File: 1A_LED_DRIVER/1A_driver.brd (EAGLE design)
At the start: 160 x 100 mm, 1 part

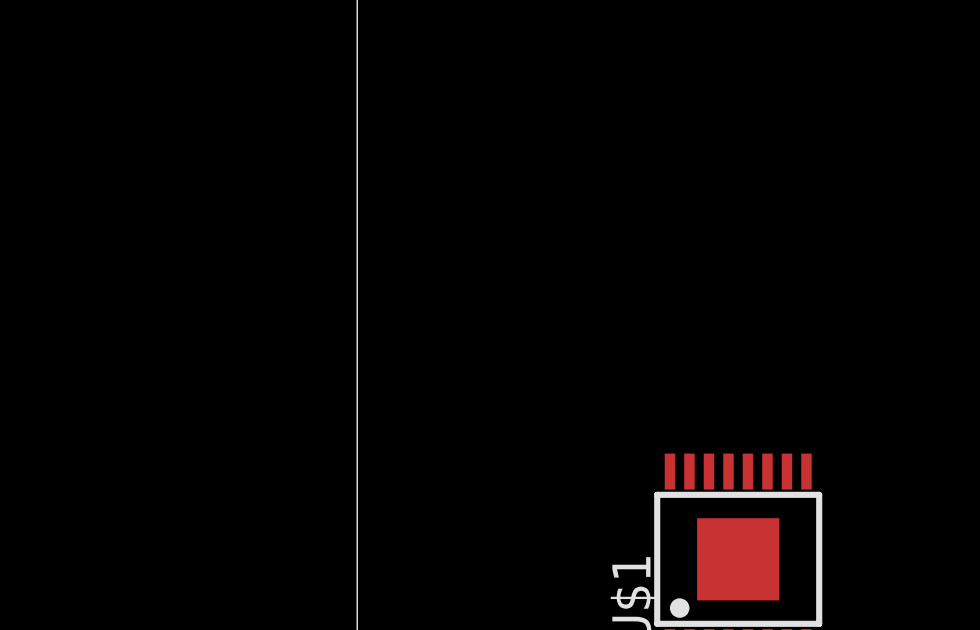
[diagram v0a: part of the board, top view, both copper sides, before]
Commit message: making new mosfet lib
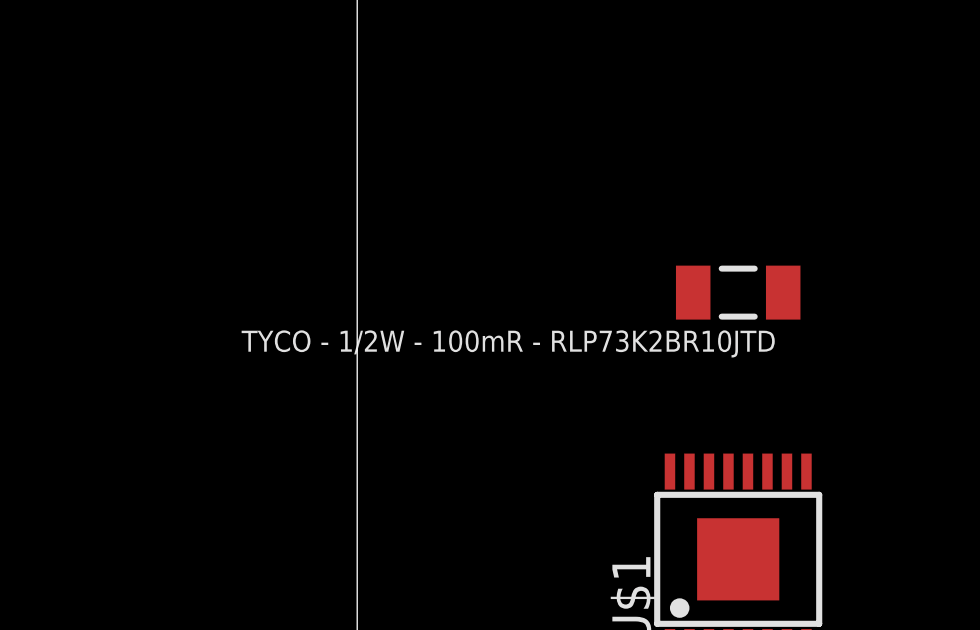
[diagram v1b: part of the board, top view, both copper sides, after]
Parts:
- added R1: TYCO - 1/2W - 100mR - RLP73K2BR10JTD, standard_passive:R1206
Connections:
- new net N$1: R1.2, U$1.13
- new net N$2: R1.1, U$1.12
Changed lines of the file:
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@@
 <elements>
 <element name="U$1" library="LT3517" package="TSSOP16_PAD" value="LT3517_TSSOP" x="12.7" y="13.97"/>
+<element name="R1" library="standard_passive" package="R1206" value="TYCO - 1/2W - 100mR - RLP73K2BR10JTD" x="12.7" y="22.86" rot="R180"/>
 </elements>
 <signals>
@@
 <contactref element="U$1" pad="17"/>
 </signal>
+<signal name="N$1">
+<contactref element="U$1" pad="13"/>
+<contactref element="R1" pad="2"/>
+<wire x1="11.2" y1="22.86" x2="12.375" y2="16.895" width="0" layer="19" extent="1-1"/>
+</signal>
+<signal name="N$2">
+<contactref element="U$1" pad="12"/>
+<contactref element="R1" pad="1"/>
+<wire x1="14.2" y1="22.86" x2="13.025" y2="16.895" width="0" layer="19" extent="1-1"/>
+</signal>
 </signals>

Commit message: schematic finished
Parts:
- added C1, C2: 0.1u, standard_passive:R0603
- added C3: 4.7u, standard_passive:R1206
- added C4: 0.22u, standard_passive:R0603
- added D1: RB060MM-60TF, DIODES:SOD123FL
- added L1: 6.8u, WE-PD:WE-PD_1260/1245/1280/1210
- added Q1: ZXMP6A13FTA, MOSFET:SOT23
- added R2, R3, R4, R5: (no value), standard_passive:R0603
- added R6: 6.04k, standard_passive:R0603
- added SV1: (no value), con-lstb:MA04-1
- added X1: 22-23-2021, con-molex:22-23-2021
- R1: value TYCO - 1/2W - 100mR - RLP73K2BR10JTD -> 100mR - 1/2W
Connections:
- new net N$10: C1.1, U$1.9
- new net N$11: R6.1, U$1.4
- new net N$3: Q1.G, U$1.14
- new net N$4: D1.A, L1.2, U$1.15, U$1.16
- new net N$5: Q1.D, X1.1
- new net N$6: R2.1, R3.2, U$1.10
- new net N$8: C2.2, U$1.6
- new net N$9: R4.2, R5.1, U$1.8
- new net PWM: SV1.3, U$1.7
- new net VIN: C3.1, L1.1, SV1.4, U$1.1, U$1.2, X1.2
- new net VREF: R4.1, U$1.11, U$1.3
- net GND: now also C1.2, C2.1, C4.2, R3.1, R5.2, R6.2, SV1.1, SV1.2, U$1.5
- net N$1: now also C3.2, C4.1, D1.C, R2.2
- net N$2: now also Q1.S
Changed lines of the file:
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@@
 <layer number="48" name="Document" color="7" fill="1" visible="yes" active="yes"/>
 <layer number="49" name="Reference" color="7" fill="1" visible="yes" active="yes"/>
+<layer number="50" name="dxf" color="7" fill="1" visible="no" active="no"/>
 <layer number="51" name="tDocu" color="7" fill="1" visible="yes" active="yes"/>
 <layer number="52" name="bDocu" color="7" fill="1" visible="yes" active="yes"/>
+<layer number="53" name="tPadExt" color="7" fill="1" visible="no" active="no"/>
+<layer number="54" name="bPadExt" color="1" fill="1" visible="no" active="no"/>
 <layer number="90" name="Modules" color="5" fill="1" visible="no" active="no"/>
 <layer number="91" name="Nets" color="2" fill="1" visible="no" active="no"/>
@@
 <layer number="97" name="Info" color="7" fill="1" visible="no" active="no"/>
 <layer number="98" name="Guide" color="6" fill="1" visible="no" active="no"/>
+<layer number="99" name="SpiceOrder" color="5" fill="1" visible="no" active="no"/>
+<layer number="250" name="Descript" color="3" fill="1" visible="no" active="no"/>
+<layer number="251" name="SMDround" color="12" fill="11" visible="no" active="no"/>
 </layers>
 <board>
@@
 <elements>
 <element name="U$1" library="LT3517" package="TSSOP16_PAD" value="LT3517_TSSOP" x="12.7" y="13.97"/>
-<element name="R1" library="standard_passive" package="R1206" value="TYCO - 1/2W - 100mR - RLP73K2BR10JTD" x="12.7" y="22.86" rot="R180"/>
+<element name="R1" library="standard_passive" package="R1206" value="100mR - 1/2W" x="12.7" y="22.86" rot="R180"/>
+<element name="Q1" library="MOSFET" package="SOT23" value="ZXMP6A13FTA" x="-2.54" y="-3.81"/>
+<element name="D1" library="DIODES" package="SOD123FL" value="RB060MM-60TF" x="-2.54" y="-10.16"/>
+<element name="X1" library="con-molex" package="22-23-2021" value="22-23-2021" x="3.81" y="-21.59">
+<attribute name="OC_FARNELL" value="1462926" x="3.81" y="-21.59" size="1.778" layer="27" display="off"/>
+<attribute name="OC_NEWARK" value="25C3832" x="3.81" y="-21.59" size="1.778" layer="27" display="off"/>
+<attribute name="MPN" value="22-23-2021" x="3.81" y="-21.59" size="1.778" layer="27" display="off"/>
+<attribute name="MF" value="MOLEX" x="3.81" y="-21.59" size="1.778" layer="27" display="off"/>
+</element>
+<element name="R2" library="standard_passive" package="R0603" value="" x="-8.89" y="-25.4"/>
+<element name="R3" library="standard_passive" package="R0603" value="" x="-13.97" y="-25.4"/>
+<element name="L1" library="WE-PD" package="WE-PD_1260/1245/1280/1210" value="6.8u" x="-22.86" y="-19.05">
+<attribute name="OC_FARNELL" value="2211534" x="-22.86" y="-19.05" size="1.778" layer="27" display="off"/>
+<attribute name="OC_NEWARK" value="44W4713" x="-22.86" y="-19.05" size="1.778" layer="27" display="off"/>
+<attribute name="SUPPLIER" value="Wuerth Elektronik" x="-22.86" y="-19.05" size="1.778" layer="27" display="off"/>
+<attribute name="MPN" value="744771006" x="-22.86" y="-19.05" size="1.778" layer="27" display="off"/>
+<attribute name="PACKAGE" value="1260" x="-22.86" y="-19.05" size="1.778" layer="27" display="off"/>
+</element>
+<element name="R4" library="standard_passive" package="R0603" value="" x="-33.02" y="-25.4"/>
+<element name="R5" library="standard_passive" package="R0603" value="" x="-38.1" y="-25.4"/>
+<element name="C1" library="standard_passive" package="R0603" value="0.1u" x="-43.18" y="-25.4"/>
+<element name="C2" library="standard_passive" package="R0603" value="0.1u" x="-48.26" y="-25.4"/>
+<element name="R6" library="standard_passive" package="R0603" value="6.04k" x="-53.34" y="-25.4"/>
+<element name="C3" library="standard_passive" package="R1206" value="4.7u" x="-58.42" y="-25.4"/>
+<element name="C4" library="standard_passive" package="R0603" value="0.22u" x="-63.5" y="-25.4"/>
+<element name="SV1" library="con-lstb" package="MA04-1" value="" x="-53.34" y="-36.83">
+<attribute name="OC_FARNELL" value="unknown" x="-53.34" y="-36.83" size="1.778" layer="27" display="off"/>
+<attribute name="OC_NEWARK" value="unknown" x="-53.34" y="-36.83" size="1.778" layer="27" display="off"/>
+<attribute name="MPN" value="" x="-53.34" y="-36.83" size="1.778" layer="27" display="off"/>
+<attribute name="MF" value="" x="-53.34" y="-36.83" size="1.778" layer="27" display="off"/>
+</element>
 </elements>
 <signals>
 <signal name="GND">
 <contactref element="U$1" pad="17"/>
+<contactref element="R3" pad="1"/>
+<contactref element="R5" pad="2"/>
+<contactref element="C2" pad="1"/>
+<contactref element="C1" pad="2"/>
+<contactref element="R6" pad="2"/>
+<contactref element="U$1" pad="5"/>
+<contactref element="C4" pad="2"/>
+<contactref element="SV1" pad="1"/>
+<contactref element="SV1" pad="2"/>
+<wire x1="-54.61" y1="-36.83" x2="-57.15" y2="-36.83" width="0" layer="19" extent="1-1"/>
+<wire x1="-52.54" y1="-25.4" x2="-54.61" y2="-36.83" width="0" layer="19" extent="1-1"/>
+<wire x1="-49.06" y1="-25.4" x2="-52.54" y2="-25.4" width="0" layer="19" extent="1-1"/>
+<wire x1="-42.38" y1="-25.4" x2="-49.06" y2="-25.4" width="0" layer="19" extent="1-1"/>
+<wire x1="-37.3" y1="-25.4" x2="-42.38" y2="-25.4" width="0" layer="19" extent="1-1"/>
+<wire x1="-62.7" y1="-25.4" x2="-52.54" y2="-25.4" width="0" layer="19" extent="1-1"/>
+<wire x1="-14.77" y1="-25.4" x2="-37.3" y2="-25.4" width="0" layer="19" extent="1-1"/>
+<wire x1="13.025" y1="11.045" x2="-14.77" y2="-25.4" width="0" layer="19" extent="1-1"/>
+<wire x1="12.7" y1="13.97" x2="13.025" y2="11.045" width="0" layer="19" extent="1-1"/>
 </signal>
 <signal name="N$1">
 <contactref element="U$1" pad="13"/>
 <contactref element="R1" pad="2"/>
+<contactref element="D1" pad="C"/>
+<contactref element="R2" pad="2"/>
+<contactref element="C3" pad="2"/>
+<contactref element="C4" pad="1"/>
+<wire x1="-56.92" y1="-25.4" x2="-64.3" y2="-25.4" width="0" layer="19" extent="1-1"/>
+<wire x1="-8.09" y1="-25.4" x2="-56.92" y2="-25.4" width="0" layer="19" extent="1-1"/>
+<wire x1="-4.165" y1="-10.16" x2="-8.09" y2="-25.4" width="0" layer="19" extent="1-1"/>
+<wire x1="12.375" y1="16.895" x2="-4.165" y2="-10.16" width="0" layer="19" extent="1-1"/>
 <wire x1="11.2" y1="22.86" x2="12.375" y2="16.895" width="0" layer="19" extent="1-1"/>
 </signal>
@@
 <contactref element="U$1" pad="12"/>
 <contactref element="R1" pad="1"/>
-<wire x1="14.2" y1="22.86" x2="13.025" y2="16.895" width="0" layer="19" extent="1-1"/>
+<contactref element="Q1" pad="S"/>
+<wire x1="13.025" y1="16.895" x2="14.2" y2="22.86" width="0" layer="19" extent="1-1"/>
+<wire x1="-1.59" y1="-4.91" x2="13.025" y2="16.895" width="0" layer="19" extent="1-1"/>
+</signal>
+<signal name="N$3">
+<contactref element="U$1" pad="14"/>
+<contactref element="Q1" pad="G"/>
+<wire x1="-3.49" y1="-4.91" x2="11.725" y2="16.895" width="0" layer="19" extent="1-1"/>
+</signal>
+<signal name="N$4">
+<contactref element="D1" pad="A"/>
+<contactref element="U$1" pad="16"/>
+<contactref element="U$1" pad="15"/>
+<contactref element="L1" pad="2"/>
+<wire x1="-0.915" y1="-10.16" x2="-17.91" y2="-19.05" width="0" layer="19" extent="1-1"/>
+<wire x1="10.425" y1="16.895" x2="-0.915" y2="-10.16" width="0" layer="19" extent="1-1"/>
+<wire x1="11.075" y1="16.895" x2="10.425" y2="16.895" width="0" layer="19" extent="1-1"/>
+</signal>
+<signal name="N$5">
+<contactref element="Q1" pad="D"/>
+<contactref element="X1" pad="1"/>
+<wire x1="-2.54" y1="-2.71" x2="2.54" y2="-21.59" width="0" layer="19" extent="1-1"/>
+</signal>
+<signal name="N$6">
+<contactref element="U$1" pad="10"/>
+<contactref element="R3" pad="2"/>
+<contactref element="R2" pad="1"/>
+<wire x1="-9.69" y1="-25.4" x2="-13.17" y2="-25.4" width="0" layer="19" extent="1-1"/>
+<wire x1="14.325" y1="16.895" x2="-9.69" y2="-25.4" width="0" layer="19" extent="1-1"/>
+</signal>
+<signal name="VIN">
+<contactref element="L1" pad="1"/>
+<contactref element="U$1" pad="1"/>
+<contactref element="U$1" pad="2"/>
+<contactref element="X1" pad="2"/>
+<contactref element="C3" pad="1"/>
+<contactref element="SV1" pad="4"/>
+<wire x1="-49.53" y1="-36.83" x2="-59.92" y2="-25.4" width="0" layer="19" extent="1-1"/>
+<wire x1="-27.81" y1="-19.05" x2="-49.53" y2="-36.83" width="0" layer="19" extent="1-1"/>
+<wire x1="5.08" y1="-21.59" x2="-27.81" y2="-19.05" width="0" layer="19" extent="1-1"/>
+<wire x1="10.425" y1="11.045" x2="5.08" y2="-21.59" width="0" layer="19" extent="1-1"/>
+<wire x1="11.075" y1="11.045" x2="10.425" y2="11.045" width="0" layer="19" extent="1-1"/>
+</signal>
+<signal name="VREF">
+<contactref element="U$1" pad="3"/>
+<contactref element="R4" pad="1"/>
+<contactref element="U$1" pad="11"/>
+<wire x1="11.725" y1="11.045" x2="-33.82" y2="-25.4" width="0" layer="19" extent="1-1"/>
+<wire x1="13.675" y1="16.895" x2="11.725" y2="11.045" width="0" layer="19" extent="1-1"/>
+</signal>
+<signal name="N$9">
+<contactref element="U$1" pad="8"/>
+<contactref element="R4" pad="2"/>
+<contactref element="R5" pad="1"/>
+<wire x1="-32.22" y1="-25.4" x2="-38.9" y2="-25.4" width="0" layer="19" extent="1-1"/>
+<wire x1="14.975" y1="11.045" x2="-32.22" y2="-25.4" width="0" layer="19" extent="1-1"/>
+</signal>
+<signal name="N$8">
+<contactref element="U$1" pad="6"/>
+<contactref element="C2" pad="2"/>
+<wire x1="13.675" y1="11.045" x2="-47.46" y2="-25.4" width="0" layer="19" extent="1-1"/>
+</signal>
+<signal name="N$10">
+<contactref element="U$1" pad="9"/>
+<contactref element="C1" pad="1"/>
+<wire x1="14.975" y1="16.895" x2="-43.98" y2="-25.4" width="0" layer="19" extent="1-1"/>
+</signal>
+<signal name="N$11">
+<contactref element="R6" pad="1"/>
+<contactref element="U$1" pad="4"/>
+<wire x1="12.375" y1="11.045" x2="-54.14" y2="-25.4" width="0" layer="19" extent="1-1"/>
+</signal>
+<signal name="PWM">
+<contactref element="SV1" pad="3"/>
+<contactref element="U$1" pad="7"/>
+<wire x1="14.325" y1="11.045" x2="-52.07" y2="-36.83" width="0" layer="19" extent="1-1"/>
 </signal>
 </signals>

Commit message: need to finish layout for the 1A regulator
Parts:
- added C5: 4.7u, standard_passive:R1206
- added C7: 100u, rcl:E5-5
- moved C4 98.1 mm to (19.7, 26.7)
- moved C3 89.7 mm to (14.6, 26.7)
- moved SV1 84.1 mm to (21.0, 2.54), turned to 180 degrees
- moved C1 80.5 mm to (24.8, 17.8)
- moved R6 80.1 mm to (18.4, 10.2), turned to 180 degrees
- moved C2 78.9 mm to (22.2, 10.2), turned to 180 degrees
- moved R5 69.6 mm to (22.9, 8.26)
- moved R4 62.5 mm to (19.7, 8.26)
- moved R3 59.4 mm to (24.8, 19.7), turned to 180 degrees
- moved R2 57.8 mm to (24.8, 21.6), turned to 180 degrees
- moved X1 52.8 mm to (30.2, 24.1), turned to 270 degrees
- moved L1 46.3 mm to (8.26, 15.2), turned to 90 degrees
- moved Q1 39.6 mm to (24.1, 25.4), turned to 270 degrees
- moved D1 38.3 mm to (14.6, 24.1), turned to 180 degrees
- moved R1 7.10 mm to (19.7, 24.1)
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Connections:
- net N$1 renamed I_P
- net N$2 renamed I_N
- net N$5 renamed I_LED
- net GND: now also C5.1, C7.-
- net VIN: now also C5.2, C7.+
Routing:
- net I_N: track 0.00 -> 7.01 mm
- net I_P: track 0.00 -> 7.01 mm
- added copper zone on layer 2, net GND
- added copper zone on layer 1, net I_N
- added copper zone on layer 1, net I_P
- added copper zone on layer 1, net N$1
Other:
- board size 160 x 100 mm -> 40 x 30 mm

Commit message: almost finished led drvier
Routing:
- net VREF: track 0.00 -> 23.1 mm, vias 0 -> 2
- net N$3: track 0.00 -> 11.4 mm, vias 0 -> 2
- net I_P: track 7.01 -> 15.8 mm, vias 0 -> 2
- net GND: track 0.00 -> 8.67 mm, vias 9 -> 18
- net N$6: track 0.00 -> 6.58 mm
- net N$9: track 0.00 -> 4.28 mm
- net N$8: track 0.00 -> 2.58 mm
- net N$11: track 0.00 -> 2.22 mm
- net N$10: track 0.00 -> 2.16 mm
- net VIN: track 0.00 -> 1.04 mm, vias 0 -> 21
- added copper zone on layer 1, net GND
- added copper zone on layer 1, net I_LED
- added copper zone on layer 1, net N$4
- added copper zone on layer 1, net VIN
- added copper zone on layer 15, net VIN
- removed copper zone on layer 1, net N$1
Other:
- board size 40 x 30 mm -> 35 x 30 mm

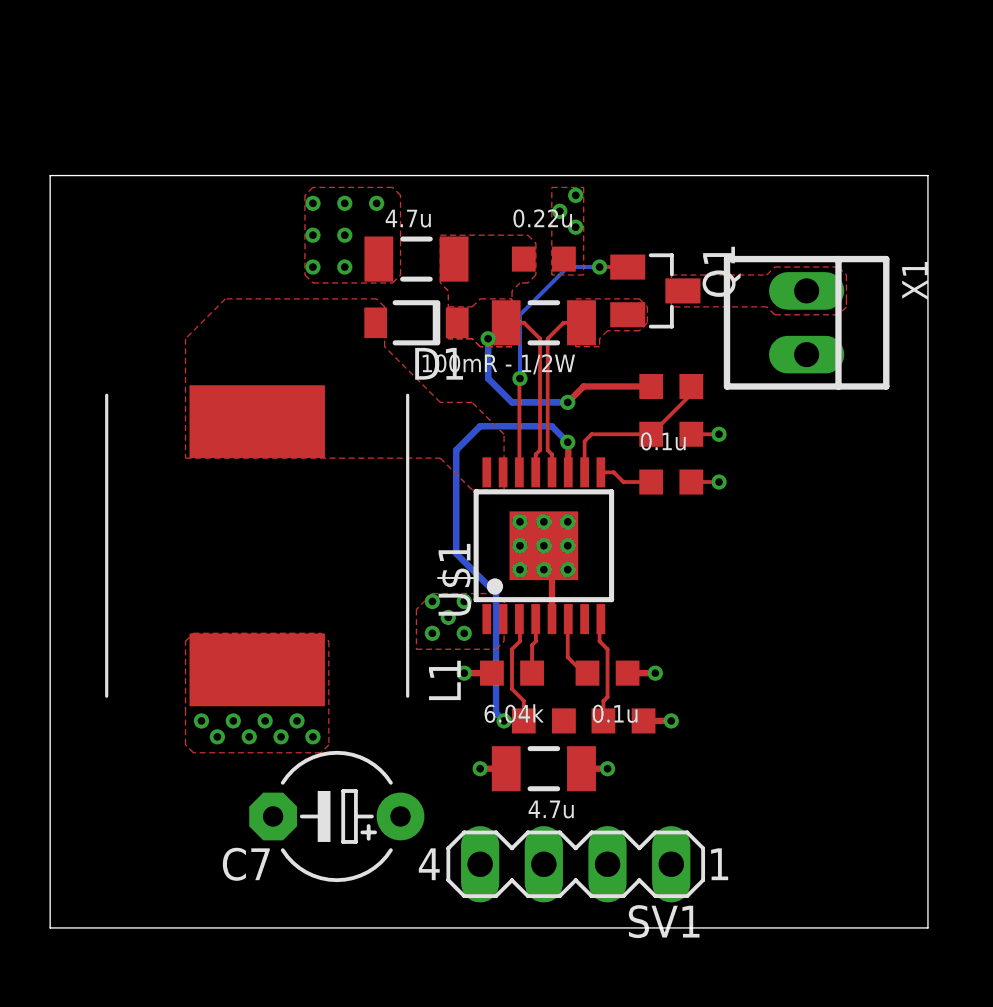
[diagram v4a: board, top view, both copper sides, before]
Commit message: finished driver, need to order stencil
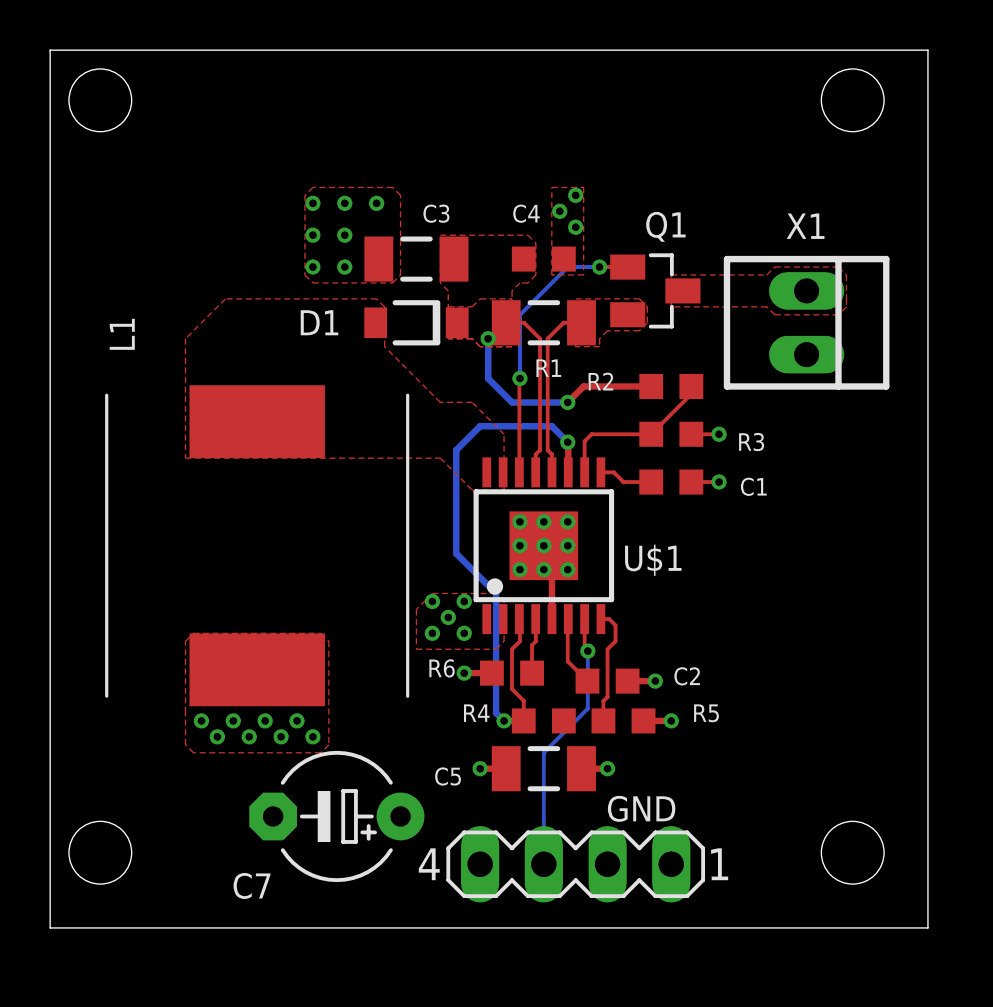
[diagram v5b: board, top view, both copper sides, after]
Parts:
- moved C2 0.32 mm to (22.2, 9.84)
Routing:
- net PWM: track 0.00 -> 10.6 mm, vias 0 -> 1
- net N$8: track 2.58 -> 3.16 mm
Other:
- board size 35 x 30 mm -> 35 x 35 mm
- board text added: "GND"
